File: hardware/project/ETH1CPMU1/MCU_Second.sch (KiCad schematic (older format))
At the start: 0 parts

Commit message: Schematic design
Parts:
- added C701, C702: 8p, Capacitor_SMD:C_0603_1608Metric_Pad1.05x0.95mm_HandSolder, symbol Device:C
- added C703, C704: 2u2, symbol Device:C
- added C705: 1u, symbol Device:C
- added J701: Conn_02x05, symbol Connector_Generic:Conn_02x05_Odd_Even
- added R701: R, symbol Device:R
- added R702, R703: 4k7, Resistor_SMD:R_0603_1608Metric_Pad1.05x0.95mm_HandSolder, symbol Device:R
- added U701: STM32H743ZI, symbol ETH1CPMU1:STM32H743ZI
- added U702: 24LC08, symbol Memory_EEPROM:24LC08
- added Y701: NX3225GD-8MHZ-STD-CRA-3, symbol Device:Crystal
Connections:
- new net: C704.1, U701.106 (VCAP_2)
- new net: R701.1, U701.138 (BOOT0)
- new net: C701.1, U701.23 (PH0,EVENTOUT,OSC_IN), Y701.1
- new net: C702.1, U701.24 (PH1,EVENTOUT,OSC_OUT), Y701.2
- new net: U701.31 (VSSA), U701.32 (VREF+)
- new net: C703.1, U701.71 (VCAP_1)
- new net +3.3VF: C705.1, J701.1 (Pin_1), R702.1, R703.1, U701.108 (VDD), U701.121 (VDDSDMMC), U701.131 (VDD), U701.143 (PDR_ON), U701.144 (VDD), U701.17 (VDD), U701.30 (VDD), U701.39 (VDD), U701.52 (VDD), U701.6 (VBAT), U701.62 (VDD), U701.72 (VDD), U701.84 (VDD), U701.95 (VDDUSB), U702.8 (VCC)
- new net DGNDF: C701.2, C702.2, J701.3 (Pin_3), J701.5 (Pin_5), R701.2, U701.107 (VSS), U701.120 (VSS), U701.130 (VSS), U701.16 (VSS), U701.38 (VSS), U701.51 (VSS), U701.61 (VSS), U701.83 (VSS), U701.94 (VSS), U702.1 (A0), U702.2 (A1), U702.3 (A2), U702.4 (GND)
- new net EEPROM_SCL: R703.2, U702.6 (SCL)
- new net EEPROM_SDA: R702.2, U702.5 (SDA)
- new net EEPROM_WP: U702.7 (WP)
- new net GND: C703.2, C704.2, C705.2
- new net MCU_NRST: J701.10 (Pin_10)
- new net TCK_SWCLK: J701.4 (Pin_4)
- new net TDI: J701.8 (Pin_8)
- new net TDO: J701.6 (Pin_6)
- new net TMS_SWDIO: J701.2 (Pin_2)
- no-connect marks 0 -> 2

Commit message: Schematic design
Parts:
- added C706, C707, C708, C709, C710, C711, C712, C713, C714, C715, C716, C717, C718: 100n, Capacitor_SMD:C_0603_1608Metric_Pad1.05x0.95mm_HandSolder, symbol Device:C
- added R704: 10k, Resistor_SMD:R_0603_1608Metric_Pad1.05x0.95mm_HandSolder, symbol Device:R
- R701: value R -> 10k
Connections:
- net +3.3VF: now also C706.1, C707.1, C708.1, C709.1, C710.1, C711.1, C712.1, C713.1, C714.1, C715.1, C716.1, C717.1, R704.1
- net DGNDF: now also C703.2, C704.2, C705.2, C706.2, C707.2, C708.2, C709.2, C710.2, C711.2, C712.2, C713.2, C714.2, C715.2, C716.2, C717.2
- net EEPROM_SCL: now also U701.11 (PF1,I2C2_SCL,FMC_A1,EVENTOUT)
- net EEPROM_SDA: now also U701.10 (PF0,I2C2_SDA,FMC_A0,EVENTOUT)
- net EEPROM_WP: now also U701.12 (PF2,I2C2_SMBA,FMC_A2,EVENTOUT)
- net GND: now also C718.2; no longer C703.2, C704.2, C705.2
- net MCU_NRST: now also U701.25 (NRST), C718.1, R704.2
- net PMU_AC0: now also U701.60 (PE9,TIM1_CH1,DFSDM1_CKOUT,UART7_RTS,QUADSPI_BK2_IO2,FMC_D6,EVENTOUT)
- net PMU_AC1: now also U701.63 (PE10,TIM1_CH2N,DFSDM1_DATIN4,UART7_CTS,QUADSPI_BK2_IO3,FMC_D7,EVENTOUT)
- net PMU_AM0: now also U701.82 (PD13,TIM4_CH2,LPTIM1_OUT,I2C4_SDA,QUADSPI_BK1_IO3,SAI2_SCK_A,FMC_A18,EVENTOUT)
- net PMU_AM1: now also U701.85 (PD14,TIM4_CH3,UART8_CTS,FMC_D0,EVENTOUT)
- net PMU_AM2: now also U701.86 (PD15,TIM4_CH4,UART8_RTS,FMC_D1,EVENTOUT)
- net PMU_CLHDETECT: now also U701.66 (PE13,TIM1_CH3,SPI4_MISO,DFSDM1_CKIN5,SAI2_FS_B,FMC_D10,LCD_DE,EVENTOUT)
- net PMU_CLLDETECT: now also U701.67 (PE14,TIM1_CH4,SPI4_MOSI,SAI2_MCLK_B,FMC_D11,LCD_CLK,EVENTOUT)
- net PMU_CPCK: now also U701.79 (PD10,DFSDM1_CKOUT,USART3_CK,FMC_D15,LCD_B3,EVENTOUT)
- net PMU_CPOH: now also U701.64 (PE11,TIM1_CH2,SPI4_NSS,DFSDM1_CKIN4,SAI2_SD_B,FMC_D8,LCD_G3,EVENTOUT)
- net PMU_CPOL: now also U701.65 (PE12,TIM1_CH3N,SPI4_SCK,DFSDM1_DATIN5,SAI2_SCK_B,FMC_D9,LCD_B4,EVENTOUT)
- net PMU_MSEL: now also U701.59 (PE8,TIM1_CH1N,DFSDM1_CKIN2,UART7_TX,QUADSPI_BK2_IO1,FMC_D5,EVENTOUT)
- net PMU_QM4: now also U701.73 (PB12,TIM1_BKIN,I2C2_SMBA,SPI2_NSS,I2S2_WS,DFSDM1_DATIN1,USART3_CK,UART5_RX,CAN2_RX,OTG_HS_ULPI_D5,ETH_MII_TXD0,ETH_RMII_TXD0,OTG_HS_ID,EVENTOUT)
- net PMU_QM5: now also U701.74 (PB13,TIM1_CH1N,SPI2_SCK,I2S2_CK,DFSDM1_CKIN1,USART3_CTS,UART5_TX,CAN2_TX,OTG_HS_ULPI_D6,ETH_MII_TXD1,ETH_RMII_TXD1,EVENTOUT,OTG_HS_VBUS)
- net PMU_STANDBY: now also U701.77 (PD8,DFSDM1_CKIN3,USART3_TX,SPDIF_RX1,FMC_D13,EVENTOUT)
- net PMU_~CS: now also U701.81 (PD12,TIM4_CH1,LPTIM1_IN1,I2C4_SCL,USART3_RTS,QUADSPI_BK1_IO1,SAI2_FS_A,FMC_A17,FMC_ALE,EVENTOUT)
- net PMU_~MOE: now also U701.80 (PD11,I2C4_SMBA,USART3_CTS,QUADSPI_BK1_IO0,SAI2_SD_A,FMC_A16,FMC_CLE,EVENTOUT)
- net PMU_~STB: now also U701.78 (PD9,DFSDM1_DATIN3,USART3_RX,FMC_D14,EVENTOUT)
- net TCK_SWCLK: now also U701.109 (PA14,JTCK-SWCLK,EVENTOUT)
- net TMS_SWDIO: now also U701.105 (PA13,JTMS-SWDIO,EVENTOUT)
- net SECOND_SCLK: now reaches U701.1 (PE2,TRACECLK,SPI4_SCK,SAI1_MCLK_A,QUADSPI_BK1_IO2,ETH_MII_TXD3,FMC_A23,EVENTOUT)
- net DAC_~SYNC: now reaches U701.110 (PA15,JTDI,TIM2_CH1,TIM2_ETR,HDMI_CEC,SPI1_NSS,I2S1_WS,SPI3_NSS,I2S3_WS,SPI6_NSS,UART4_RTS,CAN3_TX,UART7_TX,EVENTOUT)
- net DAC_SCLK: now reaches U701.111 (PC10,DFSDM1_CKIN5,SPI3_SCK,I2S3_CK,USART3_TX,UART4_TX,QUADSPI_BK1_IO1,SDMMC1_D2,DCMI_D8,LCD_R2,EVENTOUT)
- net DAC_DIN: now reaches U701.113 (PC12,TRACED3,SPI3_MOSI,I2S3_SD,USART3_CK,UART5_TX,SDMMC1_CK,DCMI_D9,EVENTOUT)
- net DAC_~LDAC: now reaches U701.114 (PD0,DFSDM1_CKIN6,DFSDM1_DATIN7,UART4_RX,CAN1_RX,FMC_D2,EVENTOUT)
- net DAC_~CLR: now reaches U701.115 (PD1,DFSDM1_DATIN6,DFSDM1_CKIN7,UART4_TX,CAN1_TX,FMC_D3,EVENTOUT)
- net DC_DAC_~CLR: now reaches U701.14 (PF4,FMC_A4,EVENTOUT,ADC3_IN14)
- net ADC_MUX_~SYNC: now reaches U701.140 (PB9,I2C4_SDA,TIM4_CH4,TIM11_CH1,I2C1_SDA,SPI2_NSS,I2S2_WS,DFSDM1_DATIN7,UART5_TX,CAN1_TX,SDMMC2_D5,I2C4_SMBA,SDMMC1_D5,DCMI_D7,LCD_B7,EVENTOUT)
- net DC_DAC_~LDAC: now reaches U701.15 (PF5,FMC_A5,EVENTOUT,ADC3_IN15)
- net DC_DAC_~SYNC: now reaches U701.18 (PF6,TIM10_CH1,SPI5_NSS,SAI1_SD_B,UART7_RX,QUADSPI_BK1_IO3,EVENTOUT,ADC3_IN4)
- net DC_DAC_SCLK: now reaches U701.19 (PF7,TIM11_CH1,SPI5_SCK,SAI1_MCLK_B,UART7_TX,QUADSPI_BK1_IO2,EVENTOUT,ADC3_IN5)
- net DC_DAC_SDO: now reaches U701.20 (PF8,SPI5_MISO,SAI1_SCK_B,UART7_RTS,TIM13_CH1,QUADSPI_BK1_IO0,EVENTOUT,ADC3_IN6)
- net DC_DAC_SDIN: now reaches U701.21 (PF9,SPI5_MOSI,SAI1_FS_B,UART7_CTS,TIM14_CH1,QUADSPI_BK1_IO1,EVENTOUT,ADC3_IN7)
- net SECOND_~SSS: now reaches U701.3 (PE4,TRACED1,SPI4_NSS,SAI1_FS_A,DFSDM1_DATIN3,FMC_A20,DCMI_D4,LCD_B0,EVENTOUT)
- net SECOND_MISO: now reaches U701.4 (PE5,TRACED2,TIM9_CH1,SPI4_MISO,SAI1_SCK_A,DFSDM1_CKIN3,FMC_A21,DCMI_D6,LCD_G0,EVENTOUT)
- net ADC_~CS: now reaches U701.40 (PA4,SPI1_NSS,I2S1_WS,SPI3_NSS,I2S3_WS,USART2_CK,SPI6_NSS,OTG_HS_SOF,DCMI_HSYNC,LCD_VSYNC,EVENTOUT,ADC1_IN4,ADC2_IN4,DAC_OUT1)
- net ADC_CLOCK: now reaches U701.41 (PA5,TIM2_CH1,TIM2_ETR,TIM8_CH1N,SPI1_SCK,I2S1_CK,SPI6_SCK,OTG_HS_ULPI_CK,LCD_R4,EVENTOUT,ADC1_IN5,ADC2_IN5,DAC_OUT2)
- net ADC_SDOA: now reaches U701.42 (PA6,TIM1_BKIN,TIM3_CH1,TIM8_BKIN,SPI1_MISO,SPI6_MISO,TIM13_CH1,MDIOS_MDC,DCMI_PIXCLK,LCD_G2,EVENTOUT,ADC1_IN6,ADC2_IN6)
- net ADC_SDI: now reaches U701.43 (PA7,TIM1_CH1N,TIM3_CH2,TIM8_CH1N,SPI1_MOSI,I2S1_SD,SPI6_MOSI,TIM14_CH1,ETH_MII_RX_DV,ETH_RMII_CRS_DV,FMC_SDNWE,EVENTOUT,ADC1_IN7,ADC2_IN7)
- net ADC_RD: now reaches U701.44 (PC4,DFSDM1_CKIN2,I2S1_MCK,SPDIF_RX2,ETH_MII_RXD0,ETH_RMII_RXD0,FMC_SDNE0,EVENTOUT,ADC1_IN14,ADC2_IN14)
- net ADC_BUSY: now reaches U701.45 (PC5,DFSDM1_DATIN2,SPDIF_RX3,ETH_MII_RXD1,ETH_RMII_RXD1,FMC_SDCKE0,EVENTOUT,ADC1_IN15,ADC2_IN15)
- net SECOND_MOSI: now reaches U701.5 (PE6,TRACED3,TIM1_BKIN2,TIM9_CH2,SPI4_MOSI,SAI1_SD_A,SAI2_MCLK_B,FMC_A22,DCMI_D7,LCD_G1,EVENTOUT)
- net PMU_CPSEL: now reaches U701.58 (PE7,TIM1_ETR,DFSDM1_DATIN2,UART7_RX,QUADSPI_BK2_IO0,FMC_D4,EVENTOUT)
- net FOURCE_SELECT: now reaches U701.68 (PE15,TIM1_BKIN,FMC_D12,LCD_R7,EVENTOUT)
- net ADC_MUX_SCLK: now reaches U701.69 (PB10,TIM2_CH3,I2C2_SCL,SPI2_SCK,I2S2_CK,DFSDM1_DATIN7,USART3_TX,QUADSPI_BK1_NCS,OTG_HS_ULPI_D3,ETH_MII_RX_ER,LCD_G4,EVENTOUT)
- net SECOND_GPIO_OUT1: now reaches U701.7 (PC13,EVENTOUT,RTC_TAMP2,RTC_TS,WKUP5)
- net ADC_MUX_SDO: now reaches U701.75 (PB14,TIM1_CH2N,TIM8_CH2N,USART1_TX,SPI2_MISO,DFSDM1_DATIN2,USART3_RTS,UART4_RTS,TIM12_CH1,SDMMC2_D0,OTG_HS_DM,EVENTOUT)
- net ADC_MUX_DIN: now reaches U701.76 (PB15,RTC_REFIN,TIM1_CH3N,TIM8_CH3N,USART1_RX,SPI2_MOSI,I2S2_SD,DFSDM1_CKIN2,UART4_CTS,TIM12_CH2,SDMMC2_D1,OTG_HS_DP,EVENTOUT)
- net SECOND_GPIO_OUT2: now reaches U701.8 (PC14,EVENTOUT,OSC32_IN)
- net R_MEASHV: now reaches U701.88 (PG3,FMC_A13,EVENTOUT)
- net R_GUARDIN: now reaches U701.89 (PG4,FMC_A14,FMC_BA0,EVENTOUT)
- net SECOND_STATUS_IN: now reaches U701.9 (PC15,EVENTOUT,OSC32_OUT)
- net R_GND: now reaches U701.90 (PG5,FMC_A15,FMC_BA1,EVENTOUT)
- net R_MEASIL: now reaches U701.91 (PG6,FMC_NE3,DCMI_D12,LCD_R7,EVENTOUT)
- net R_MEASVL: now reaches U701.92 (PG7,SAI1_MCLK_A,USART6_CK,FMC_INT,DCMI_D13,LCD_CLK,EVENTOUT)
- net R_GUARD: now reaches U701.93 (PG8,SPI6_NSS,SPDIF_RX2,USART6_RTS,ETH_PPS_OUT,FMC_SDCLK,LCD_G7,EVENTOUT)
- net TDI: no longer names the net of J701.8 (Pin_8)
- net TDO: no longer names the net of J701.6 (Pin_6)
- no-connect marks 2 -> 6
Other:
- moved on the sheet: C701, C702, Y701

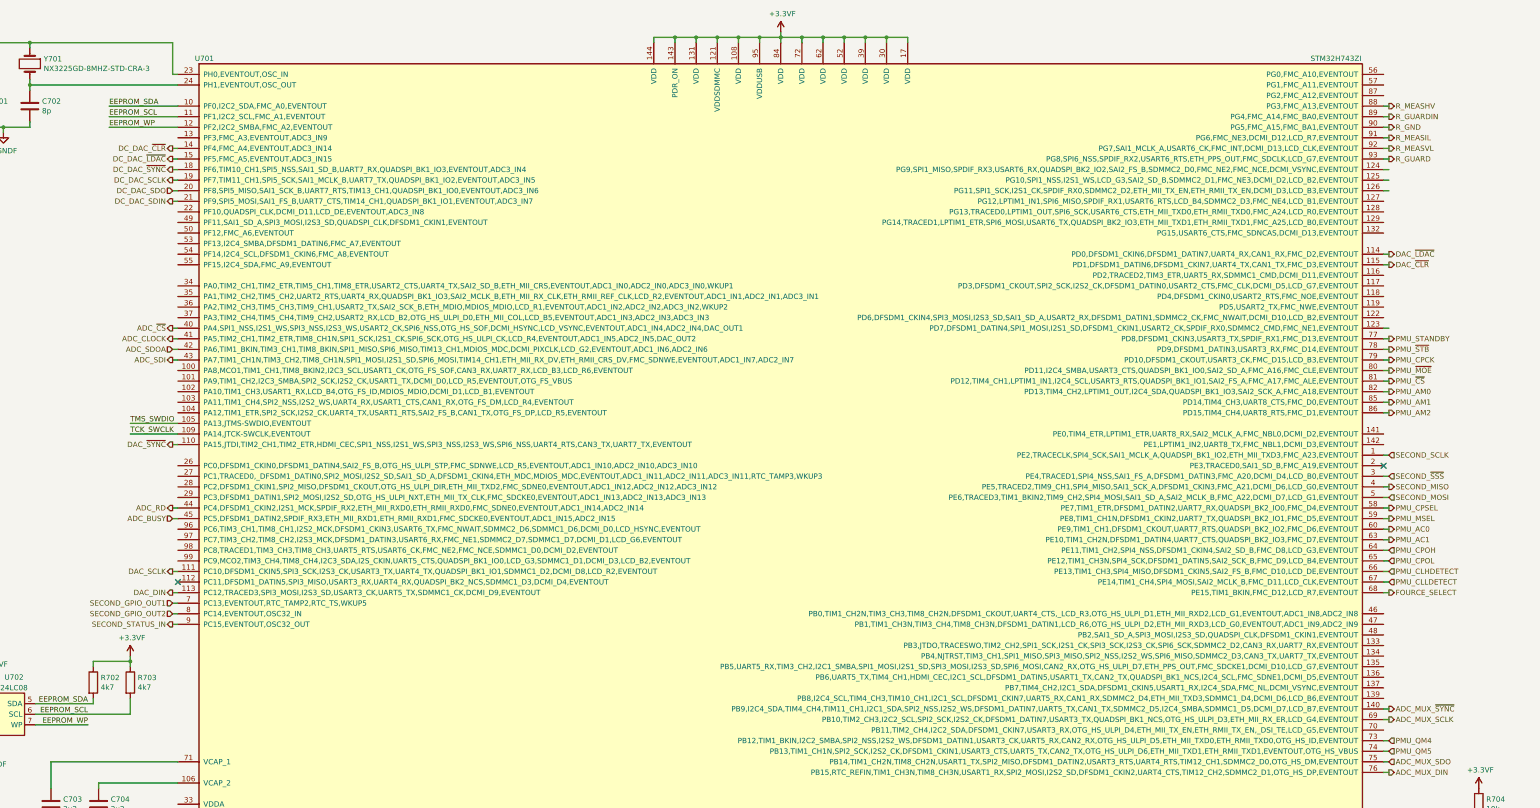
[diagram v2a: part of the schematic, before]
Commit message: Function generator schematic design.
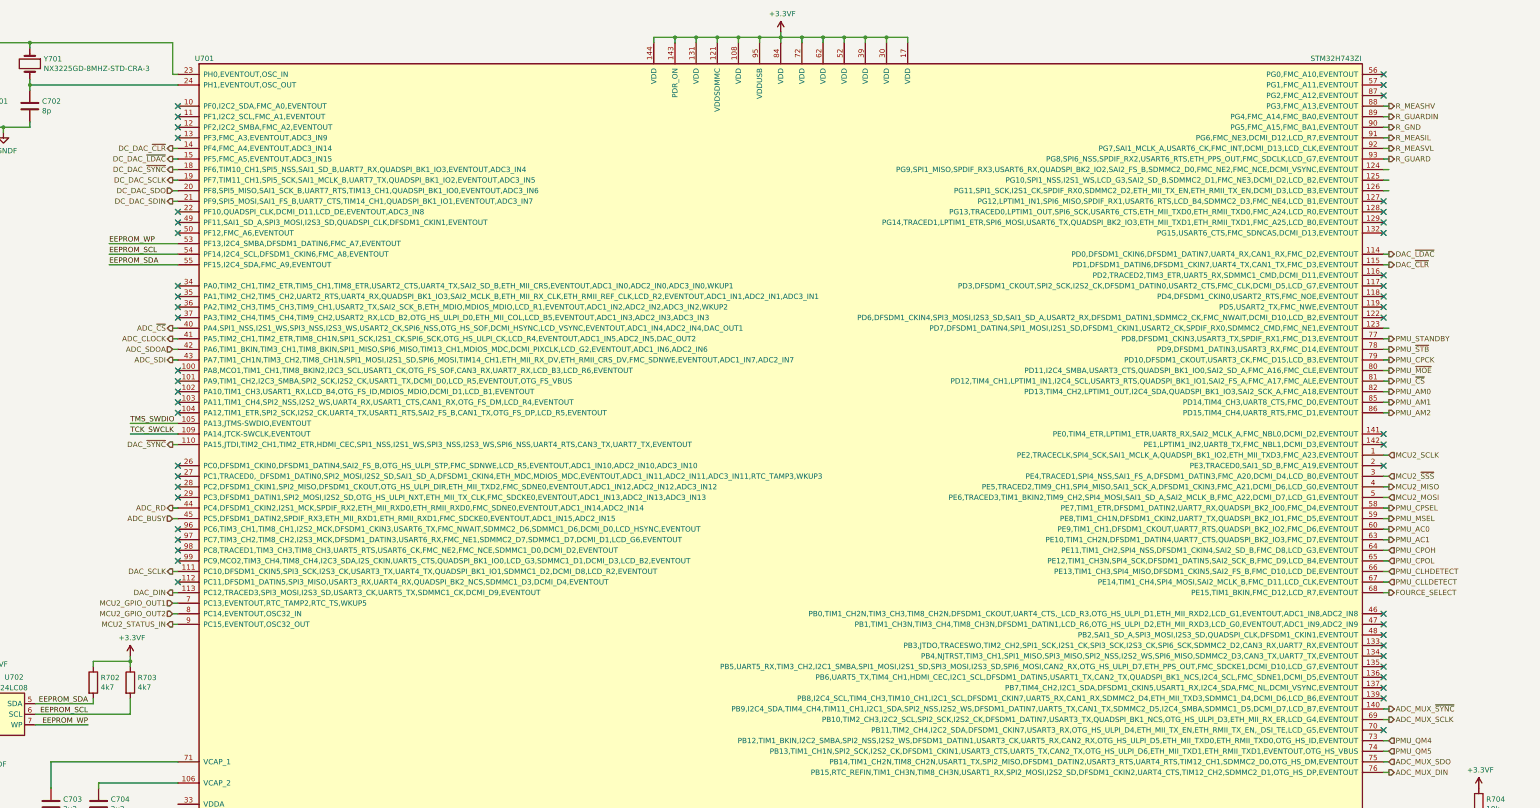
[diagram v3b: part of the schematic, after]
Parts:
- C703, C704: footprint (none) -> Capacitor_SMD:C_0805_2012Metric_Pad1.15x1.40mm_HandSolder
- C705: footprint (none) -> Capacitor_SMD:C_0603_1608Metric_Pad1.05x0.95mm_HandSolder
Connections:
- net EEPROM_SCL: now also U701.54 (PF14,I2C4_SCL,DFSDM1_CKIN6,FMC_A8,EVENTOUT); no longer U701.11 (PF1,I2C2_SCL,FMC_A1,EVENTOUT)
- net EEPROM_SDA: now also U701.55 (PF15,I2C4_SDA,FMC_A9,EVENTOUT); no longer U701.10 (PF0,I2C2_SDA,FMC_A0,EVENTOUT)
- net EEPROM_WP: now also U701.53 (PF13,I2C4_SMBA,DFSDM1_DATIN6,FMC_A7,EVENTOUT); no longer U701.12 (PF2,I2C2_SMBA,FMC_A2,EVENTOUT)
- net SECOND_GPIO_OUT1 renamed MCU2_GPIO_OUT1
- net SECOND_GPIO_OUT2 renamed MCU2_GPIO_OUT2
- net SECOND_MISO renamed MCU2_MISO
- net SECOND_MOSI renamed MCU2_MOSI
- net SECOND_SCLK renamed MCU2_SCLK
- net SECOND_STATUS_IN renamed MCU2_STATUS_IN
- net SECOND_~SSS renamed MCU2_~SSS
- no-connect marks 6 -> 54
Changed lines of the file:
@@
 $Descr A3 16535 11693
 encoding utf-8
-Sheet 14 14
+Sheet 13 15
 Title ""
 Date ""
@@
 F 0 "C704" H 2265 8246 50  0000 L CNN
 F 1 "2u2" H 2265 8155 50  0000 L CNN
-F 2 "" H 2188 8050 50  0001 C CNN
+F 2 "Capacitor_SMD:C_0805_2012Metric_Pad1.15x1.40mm_HandSolder" H 2188 8050 50  0001 C CNN
 F 3 "~" H 2150 8200 50  0001 C CNN
 	1    2150 8200
@@
 F 0 "C703" H 1815 8246 50  0000 L CNN
 F 1 "2u2" H 1815 8155 50  0000 L CNN
-F 2 "" H 1738 8050 50  0001 C CNN
+F 2 "Capacitor_SMD:C_0805_2012Metric_Pad1.15x1.40mm_HandSolder" H 1738 8050 50  0001 C CNN
 F 3 "~" H 1700 8200 50  0001 C CNN
 	1    1700 8200
@@
 F 0 "C705" H 2965 9096 50  0000 L CNN
 F 1 "1u" H 2965 9005 50  0000 L CNN
-F 2 "" H 2888 8900 50  0001 C CNN
+F 2 "Capacitor_SMD:C_0603_1608Metric_Pad1.05x0.95mm_HandSolder" H 2888 8900 50  0001 C CNN
 F 3 "~" H 2850 9050 50  0001 C CNN
 	1    2850 9050
@@
 $EndComp
 Text HLabel 14350 5100 2    50   Input ~ 0
-SECOND_~SSS
+MCU2_~SSS
 Text HLabel 14350 5200 2    50   Output ~ 0
-SECOND_MISO
+MCU2_MISO
 Text HLabel 14350 5300 2    50   Input ~ 0
-SECOND_MOSI
+MCU2_MOSI
 Text HLabel 14350 4900 2    50   Input ~ 0
-SECOND_SCLK
+MCU2_SCLK
 Text HLabel 2850 6300 0    50   Input ~ 0
-SECOND_GPIO_OUT1
+MCU2_GPIO_OUT1
 Text HLabel 2850 6500 0    50   Output ~ 0
-SECOND_STATUS_IN
+MCU2_STATUS_IN
 Text HLabel 2850 6400 0    50   Input ~ 0
-SECOND_GPIO_OUT2
+MCU2_GPIO_OUT2
 Wire Wire Line
 	14350 4900 14300 4900
@@
 	2850 2200 2900 2200
 Wire Wire Line
-	2900 1600 2250 1600
-Wire Wire Line
-	2900 1700 2250 1700
-Text Label 2250 1600 0    50   ~ 0
+	2900 3100 2250 3100
+Wire Wire Line
+	2900 3000 2250 3000
+Text Label 2250 3100 0    50   ~ 0
 EEPROM_SDA
-Text Label 2250 1700 0    50   ~ 0
+Text Label 2250 3000 0    50   ~ 0
 EEPROM_SCL
-Text Label 2250 1800 0    50   ~ 0
+Text Label 2250 2900 0    50   ~ 0
 EEPROM_WP
 Wire Wire Line
-	2250 1800 2900 1800
+	2250 2900 2900 2900
 Wire Wire Line
 	2900 2000 2850 2000
@@
 Wire Wire Line
 	15200 8400 14300 8400
+NoConn ~ 2900 1600
+NoConn ~ 2900 1700
+NoConn ~ 2900 1800
+NoConn ~ 2900 1900
+NoConn ~ 2900 2600
+NoConn ~ 2900 2700
+NoConn ~ 2900 2800
+NoConn ~ 2900 3300
+NoConn ~ 2900 3400
+NoConn ~ 2900 3500
+NoConn ~ 2900 3600
+NoConn ~ 2900 4100
+NoConn ~ 2900 4200
+NoConn ~ 2900 4300
+NoConn ~ 2900 4400
+NoConn ~ 2900 4500
+NoConn ~ 2900 5000
+NoConn ~ 2900 5100
+NoConn ~ 2900 5200
+NoConn ~ 2900 5300
+NoConn ~ 2900 5600
+NoConn ~ 2900 5700
+NoConn ~ 2900 5800
+NoConn ~ 2900 5900
+NoConn ~ 14300 1300
+NoConn ~ 14300 1400
+NoConn ~ 14300 1500
+NoConn ~ 14300 2500
+NoConn ~ 14300 2600
+NoConn ~ 14300 2700
+NoConn ~ 14300 2800
+NoConn ~ 14300 3200
+NoConn ~ 14300 3300
+NoConn ~ 14300 3400
+NoConn ~ 14300 3500
+NoConn ~ 14300 3600
+NoConn ~ 14300 4700
+NoConn ~ 14300 4800
+NoConn ~ 14300 6400
+NoConn ~ 14300 6500
+NoConn ~ 14300 6600
+NoConn ~ 14300 6700
+NoConn ~ 14300 6800
+NoConn ~ 14300 6900
+NoConn ~ 14300 7000
+NoConn ~ 14300 7100
+NoConn ~ 14300 7200
+NoConn ~ 14300 7500
 $EndSCHEMATC

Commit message: Function generator schematic development.
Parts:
- R701: footprint (none) -> Resistor_SMD:R_0603_1608Metric_Pad1.05x0.95mm_HandSolder
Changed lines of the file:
@@
 EESchema Schematic File Version 4
-LIBS:ETH1CPMU1-cache
 EELAYER 30 0
 EELAYER END
@@
 F 0 "R701" H 14470 9046 50  0000 L CNN
 F 1 "10k" H 14470 8955 50  0000 L CNN
-F 2 "" V 14330 9000 50  0001 C CNN
+F 2 "Resistor_SMD:R_0603_1608Metric_Pad1.05x0.95mm_HandSolder" V 14330 9000 50  0001 C CNN
 F 3 "~" H 14400 9000 50  0001 C CNN
 	1    14400 9000

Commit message: New footprint development, changes in schematics.
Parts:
- J1301: renamed from J701; footprint (none) -> Connector_PinHeader_1.27mm:PinHeader_2x05_P1.27mm_Vertical
- U1301: renamed from U701; footprint (none) -> ETH1CPMU1:TQFP-144_20x20mm_P0.5mm
- Y1301: renamed from Y701; footprint (none) -> ETH1CPMU1:NX3225GD
- renumbered C701 to C1301, C702 to C1302, C703 to C1303, C704 to C1304, C718 to C1305, C705 to C1306, C706 to C1307, C707 to C1308, C708 to C1309, C709 to C1310, C710 to C1311, C711 to C1312, C712 to C1313, C713 to C1314, C714 to C1315, C715 to C1316, C716 to C1317, C717 to C1318, R702 to R1301, R703 to R1302, R704 to R1303, R701 to R1304, U702 to U1302
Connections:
- net PMU_QM4: no longer names the net of U1301.73 (PB12,TIM1_BKIN,I2C2_SMBA,SPI2_NSS,I2S2_WS,DFSDM1_DATIN1,USART3_CK,UART5_RX,CAN2_RX,OTG_HS_ULPI_D5,ETH_MII_TXD0,ETH_RMII_TXD0,OTG_HS_ID,EVENTOUT)
- net PMU_QM5: no longer names the net of U1301.74 (PB13,TIM1_CH1N,SPI2_SCK,I2S2_CK,DFSDM1_CKIN1,USART3_CTS,UART5_TX,CAN2_TX,OTG_HS_ULPI_D6,ETH_MII_TXD1,ETH_RMII_TXD1,EVENTOUT,OTG_HS_VBUS)
- no-connect marks 54 -> 56
